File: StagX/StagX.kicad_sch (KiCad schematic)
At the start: 2 parts

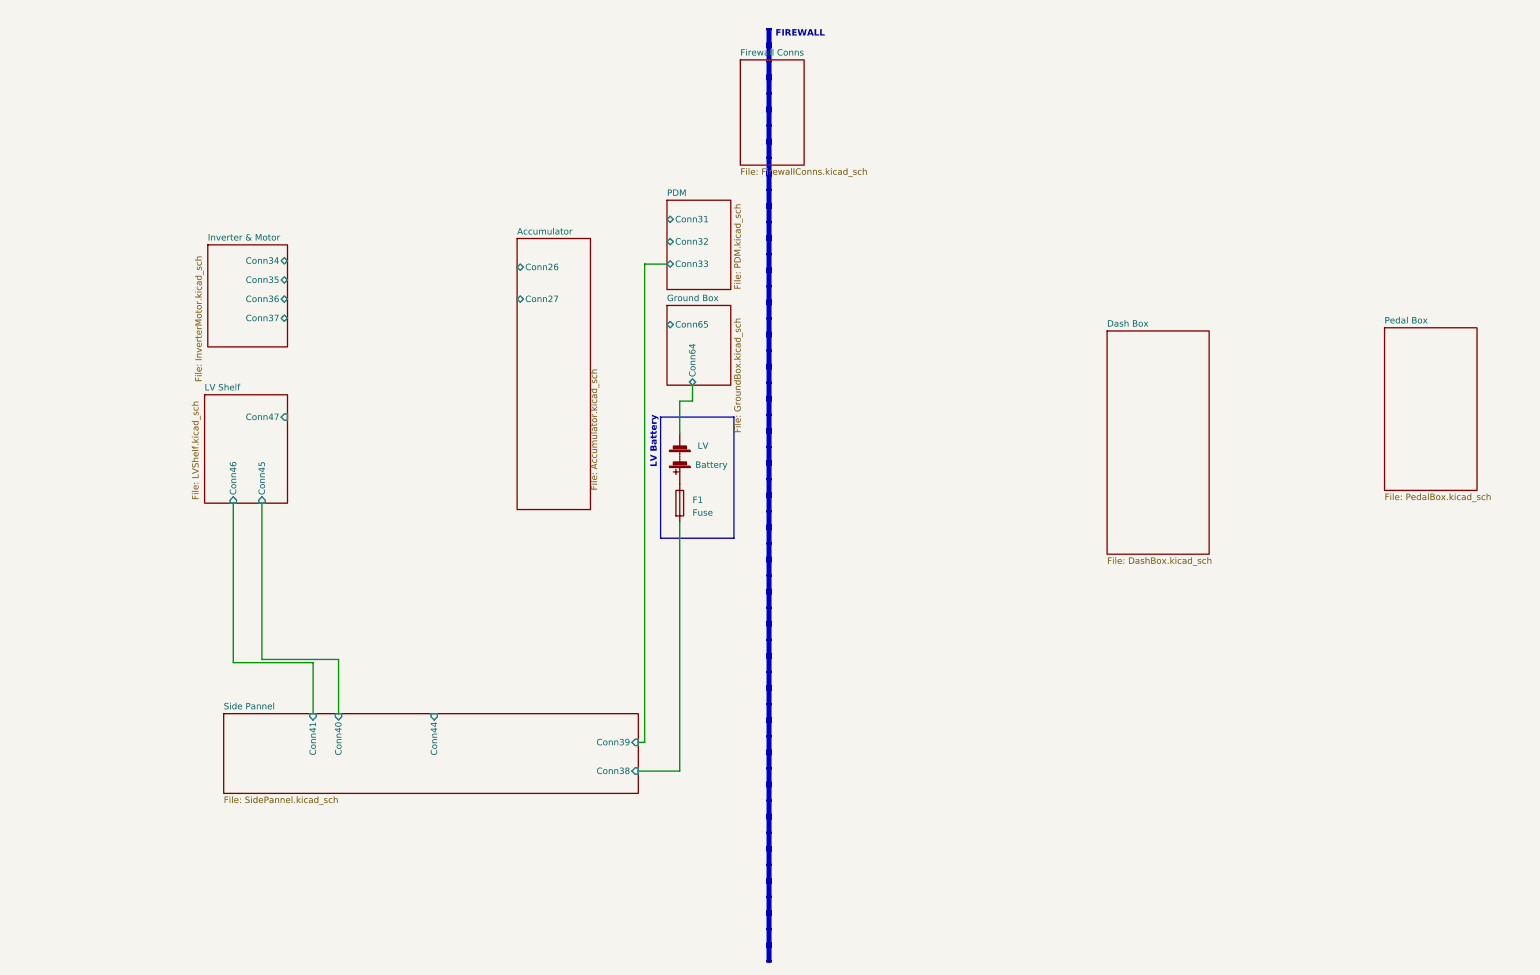
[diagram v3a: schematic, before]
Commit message: feat(RearLoom): completed Rear Electronics Box
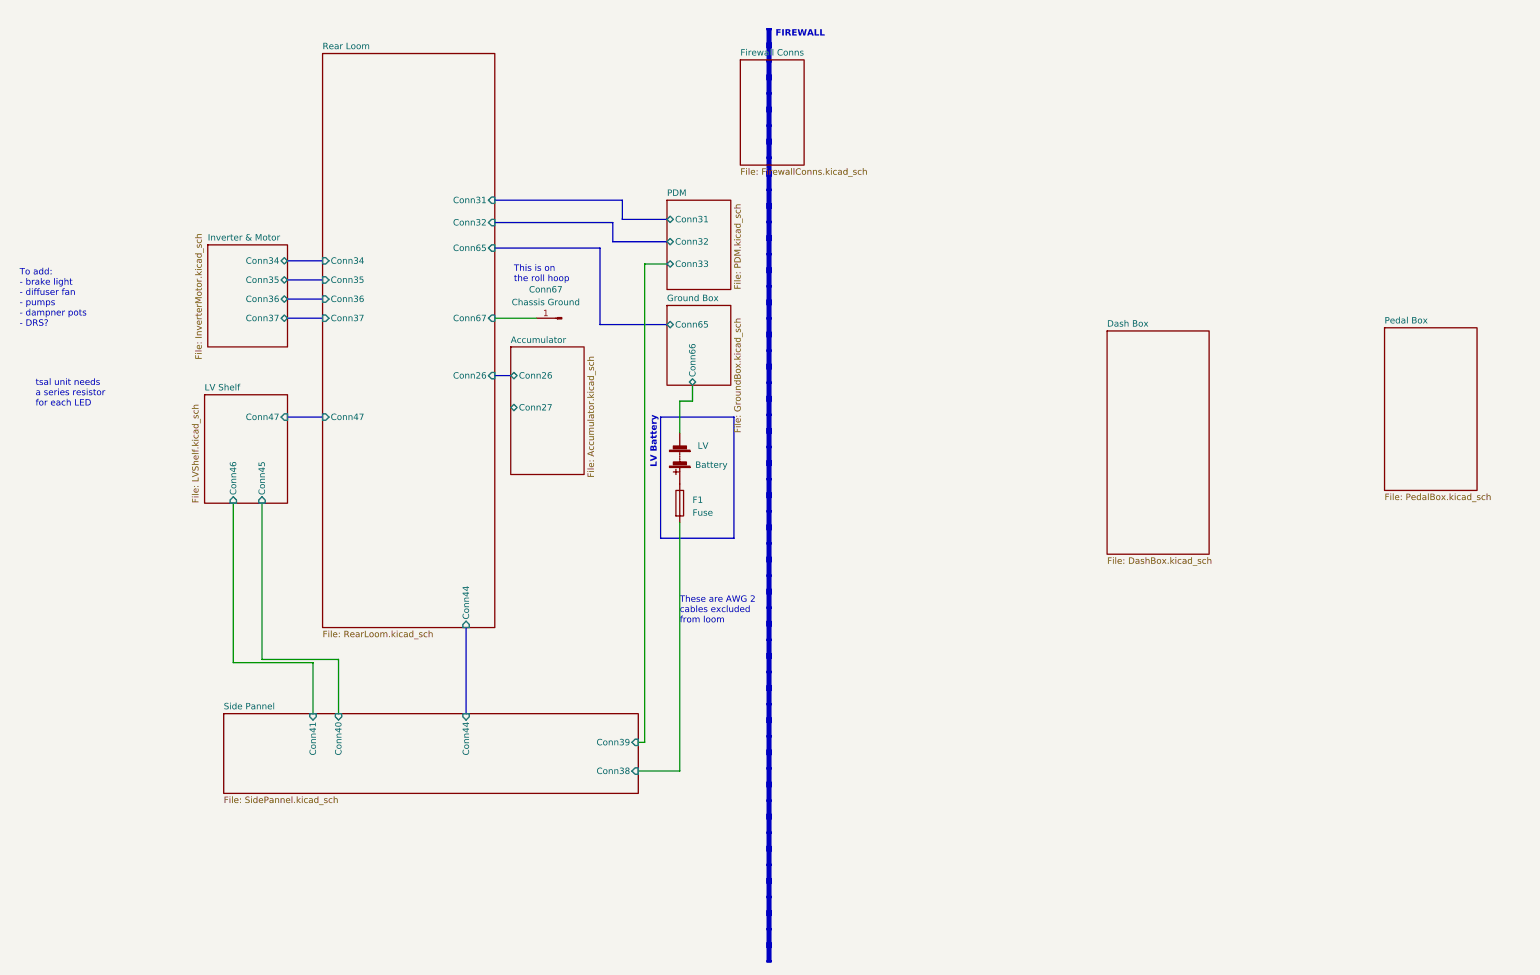
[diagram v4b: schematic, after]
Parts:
- added Conn67: Chassis Ground, symbol Connector:Conn_01x01_Pin
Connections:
- net Ground Box/Conn64 renamed Ground Box/Conn66
- new net Rear Loom/Conn67: Conn67.1 (Pin_1)
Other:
- added sheet Rear Loom (RearLoom.kicad_sch)
- sheet Ground Box ports: added Conn66; removed Conn64
- note added: "These are AWG 2 cables excluded from loom"
- note added: "This is on the roll hoop"
- note added: "To add: - brake light - diffuser fan - pumps - dampner pots - DRS?"
- note added: "tsal unit needs a series resistor for each LED"
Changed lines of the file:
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@@
     (comment 4 "N/A")
   )
+  (bus (pts (xy 99.06 51.435) (xy 99.06 55.245))
+    (stroke (width 0) (type default))
+  )
+  (bus (pts (xy 75.565 56.515) (xy 96.52 56.515))
+    (stroke (width 0) (type default))
+  )
   (wire (pts (xy 112.395 86.995) (xy 114.935 86.995))
     (stroke (width 0) (type default))
   )
+  (bus (pts (xy 34.29 66.675) (xy 41.275 66.675))
+    (stroke (width 0) (type default))
+  )
   (wire (pts (xy 39.37 149.225) (xy 39.37 139.065))
     (stroke (width 0) (type default))
   )
+  (bus (pts (xy 99.06 55.245) (xy 109.855 55.245))
+    (stroke (width 0) (type default))
+  )
   (wire (pts (xy 29.21 138.43) (xy 29.21 107.315))
     (stroke (width 0) (type default))
   )
+  (bus (pts (xy 34.29 59.055) (xy 41.275 59.055))
+    (stroke (width 0) (type default))
+  )
+  (bus (pts (xy 34.29 90.17) (xy 41.275 90.17))
+    (stroke (width 0) (type default))
+  )
+  (bus (pts (xy 75.565 51.435) (xy 99.06 51.435))
+    (stroke (width 0) (type default))
+  )
+  (bus (pts (xy 100.965 46.99) (xy 100.965 50.8))
+    (stroke (width 0) (type default))
+  )
   (wire (pts (xy 112.395 160.655) (xy 104.14 160.655))
     (stroke (width 0) (type default))
@@
     (stroke (width 0) (type default))
   )
+  (bus (pts (xy 69.85 132.08) (xy 69.85 149.225))
+    (stroke (width 0) (type default))
+  )
   (wire (pts (xy 23.495 107.315) (xy 23.495 139.065))
     (stroke (width 0) (type default))
   )
+  (bus (pts (xy 75.565 46.99) (xy 100.965 46.99))
+    (stroke (width 0) (type default))
+  )
+  (bus (pts (xy 96.52 56.515) (xy 96.52 71.755))
+    (stroke (width 0) (type default))
+  )
   (wire (pts (xy 44.45 138.43) (xy 29.21 138.43))
     (stroke (width 0) (type default))
   )
+  (bus (pts (xy 100.965 50.8) (xy 109.855 50.8))
+    (stroke (width 0) (type default))
+  )
   (wire (pts (xy 112.395 111.125) (xy 112.395 160.655))
     (stroke (width 0) (type default))
   )
+  (bus (pts (xy 75.565 81.915) (xy 78.74 81.915))
+    (stroke (width 0) (type default))
+  )
+  (bus (pts (xy 34.29 70.485) (xy 41.275 70.485))
+    (stroke (width 0) (type default))
+  )
   (wire (pts (xy 39.37 139.065) (xy 23.495 139.065))
     (stroke (width 0) (type default))
@@
   )
   (wire (pts (xy 105.41 59.69) (xy 109.855 59.69))
+    (stroke (width 0) (type default))
+  )
+  (bus (pts (xy 34.29 62.865) (xy 41.275 62.865))
+    (stroke (width 0) (type default))
+  )
+  (bus (pts (xy 96.52 71.755) (xy 109.855 71.755))
+    (stroke (width 0) (type default))
+  )
+  (wire (pts (xy 75.565 70.485) (xy 83.82 70.485))
     (stroke (width 0) (type default))
   )
@@
     (fill (type none))
   )
+  (text "To add:\n- brake light\n- diffuser fan\n- pumps\n- dampner pots\n- DRS?\n"
+    (at -19.05 72.39 0)
+    (effects (font (size 1.27 1.27)) (justify left bottom))
+  )
+  (text "This is on\nthe roll hoop" (at 79.375 63.5 0)
+    (effects (font (size 1.27 1.27)) (justify left bottom))
+  )
+  (text "These are AWG 2\ncables excluded\nfrom loom" (at 112.395 131.445 0)
+    (effects (font (size 1.27 1.27)) (justify left bottom))
+  )
   (text "LV Battery" (at 107.95 100.33 90)
     (effects (font (size 1.27 1.27) bold (color 0 0 0 1)) (justify left bottom))
@@
   (text "FIREWALL" (at 131.445 14.605 0)
     (effects (font (size 1.27 1.27) (thickness 0.254) bold (color 255 0 0 1)) (justify left bottom))
+  )
+  (text "tsal unit needs \na series resistor\nfor each LED" (at -15.875 88.265 0)
+    (effects (font (size 1.27 1.27)) (justify left bottom))
   )
   (symbol (lib_id "Device:Fuse") (at 112.395 107.315 0) (unit 1)
@@
     )
   )
+  (symbol (lib_id "Connector:Conn_01x01_Pin") (at 88.9 70.485 180) (unit 1)
+    (in_bom yes) (on_board yes) (dnp no)
+    (property "Reference" "Conn67" (at 85.725 64.77 0)
+      (effects (font (size 1.27 1.27)))
+    )
+    (property "Value" "Chassis Ground" (at 85.725 67.31 0)
+      (effects (font (size 1.27 1.27)))
+    )
+    (property "Footprint" "" (at 88.9 70.485 0)
+      (effects (font (size 1.27 1.27)) hide)
+    )
+    (property "Datasheet" "~" (at 88.9 70.485 0)
+      (effects (font (size 1.27 1.27)) hide)
+    )
+    (pin "1")
+    (instances
+      (project "StagX"
+        (path "/f802a14a-9970-4775-97a5-629bebb8e9f9"
+          (reference "Conn67") (unit 1)
+        )
+      )
+    )
+  )
   (symbol (lib_id "Device:Battery") (at 112.395 98.425 180) (unit 1)
     (in_bom yes) (on_board yes) (dnp no)
@@
       (effects (font (size 1.27 1.27)) (justify left bottom))
     )
-    (property "Sheetfile" "InverterMotor.kicad_sch" (at 15.875 83.185 90)
+    (property "Sheetfile" "InverterMotor.kicad_sch" (at 15.875 78.74 90)
       (effects (font (size 1.27 1.27)) (justify left top))
     )
@@
       (effects (font (size 1.27 1.27)) (justify left bottom))
     )
-    (property "Sheetfile" "LVShelf.kicad_sch" (at 15.24 106.68 90)
+    (property "Sheetfile" "LVShelf.kicad_sch" (at 15.24 107.315 90)
       (effects (font (size 1.27 1.27)) (justify left top))
     )
@@
     )
   )
-  (sheet (at 80.01 54.61) (size 14.605 53.975)
-    (stroke (width 0.1524) (type solid) (color 255 0 0 1))
-    (fill (color 0 0 0 0.0000))
-    (property "Sheetname" "Accumulator" (at 80.01 53.975 0)
-      (effects (font (size 1.27 1.27)) (justify left bottom))
-    )
-    (property "Sheetfile" "Accumulator.kicad_sch" (at 94.615 104.775 90)
-      (effects (font (size 1.27 1.27)) (justify left top))
-    )
-    (pin "Conn26" bidirectional (at 80.01 60.325 180)
-      (effects (font (size 1.27 1.27)) (justify left))
-    )
-    (pin "Conn27" bidirectional (at 80.01 66.675 180)
+  (sheet (at 78.74 76.2) (size 14.605 25.4)
+    (stroke (width 0.1524) (type solid) (color 255 0 0 1))
+    (fill (color 0 0 0 0.0000))
+    (property "Sheetname" "Accumulator" (at 78.74 75.565 0)
+      (effects (font (size 1.27 1.27)) (justify left bottom))
+    )
+    (property "Sheetfile" "Accumulator.kicad_sch" (at 93.98 102.235 90)
+      (effects (font (size 1.27 1.27)) (justify left top))
+    )
+    (pin "Conn26" bidirectional (at 78.74 81.915 180)
+      (effects (font (size 1.27 1.27)) (justify left))
+    )
+    (pin "Conn27" bidirectional (at 78.74 88.265 180)
       (effects (font (size 1.27 1.27)) (justify left))
     )
@@
       (effects (font (size 1.27 1.27)) (justify right))
     )
-    (pin "Conn44" input (at 63.5 149.225 90)
+    (pin "Conn44" input (at 69.85 149.225 90)
       (effects (font (size 1.27 1.27)) (justify right))
     )
@@
     )
   )
+  (sheet (at 41.275 17.78) (size 34.29 114.3) (fields_autoplaced)
+    (stroke (width 0.1524) (type solid) (color 0 0 255 1))
+    (fill (color 0 0 0 0.0000))
+    (property "Sheetname" "Rear Loom" (at 41.275 17.0684 0)
+      (effects (font (size 1.27 1.27)) (justify left bottom))
+    )
+    (property "Sheetfile" "RearLoom.kicad_sch" (at 41.275 132.6646 0)
+      (effects (font (size 1.27 1.27)) (justify left top))
+    )
+    (pin "Conn44" input (at 69.85 132.08 270)
+      (effects (font (size 1.27 1.27)) (justify left))
+    )
+    (pin "Conn34" input (at 41.275 59.055 180)
+      (effects (font (size 1.27 1.27)) (justify left))
+    )
+    (pin "Conn36" input (at 41.275 66.675 180)
+      (effects (font (size 1.27 1.27)) (justify left))
+    )
+    (pin "Conn47" input (at 41.275 90.17 180)
+      (effects (font (size 1.27 1.27)) (justify left))
+    )
+    (pin "Conn37" input (at 41.275 70.485 180)
+      (effects (font (size 1.27 1.27)) (justify left))
+    )
+    (pin "Conn26" input (at 75.565 81.915 0)
+      (effects (font (size 1.27 1.27)) (justify right))
+    )
+    (pin "Conn35" input (at 41.275 62.865 180)
+      (effects (font (size 1.27 1.27)) (justify left))
+    )
+    (pin "Conn31" input (at 75.565 46.99 0)
+      (effects (font (size 1.27 1.27)) (justify right))
+    )
+    (pin "Conn32" input (at 75.565 51.435 0)
+      (effects (font (size 1.27 1.27)) (justify right))
+    )
+    (pin "Conn65" input (at 75.565 56.515 0)
+      (effects (font (size 1.27 1.27)) (justify right))
+    )
+    (pin "Conn67" input (at 75.565 70.485 0)
+      (effects (font (size 1.27 1.27)) (justify right))
+    )
+    (instances
+      (project "StagX"
+        (path "/f802a14a-9970-4775-97a5-629bebb8e9f9" (page "12"))
+      )
+    )
+  )
   (sheet (at 109.855 67.945) (size 12.7 15.875)
     (stroke (width 0.1524) (type solid) (color 255 0 0 1))
@@
       (effects (font (size 1.27 1.27)) (justify left top))
     )
-    (pin "Conn64" bidirectional (at 114.935 83.82 270)
-      (effects (font (size 1.27 1.27)) (justify left))
-    )
+    (pin "Conn66" bidirectional (at 114.935 83.82 270)
+      (effects (font (size 1.27 1.27)) (justify left))
+    )

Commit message: feat(RearLoom): completed Inverter, Motor and Resolver sheet
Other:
- sheet Inverter & Motor ports: added Conn68; removed none
- sheet Rear Loom ports: added Conn68; removed none
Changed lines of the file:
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@@
+    (stroke (width 0) (type default))
+  )
+  (bus (pts (xy 34.29 73.66) (xy 41.275 73.66))
     (stroke (width 0) (type default))
   )
@@
       (effects (font (size 1.27 1.27)) (justify right))
     )
+    (pin "Conn68" bidirectional (at 34.29 73.66 0)
+      (effects (font (size 1.27 1.27)) (justify right))
+    )
     (instances
       (project "StagX"
@@
       (effects (font (size 1.27 1.27)) (justify right))
     )
-    (instances
+    (pin "Conn68" input (at 41.275 73.66 180)
+      (effects (font (size 1.27 1.27)) (justify left))
+    )
+    (instances

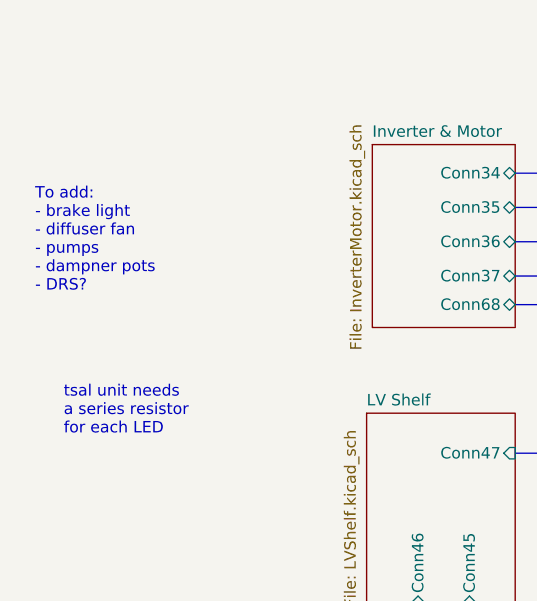
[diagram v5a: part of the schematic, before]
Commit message: feat(RearLoom): progress with Rear Loom. Miising Power and GND
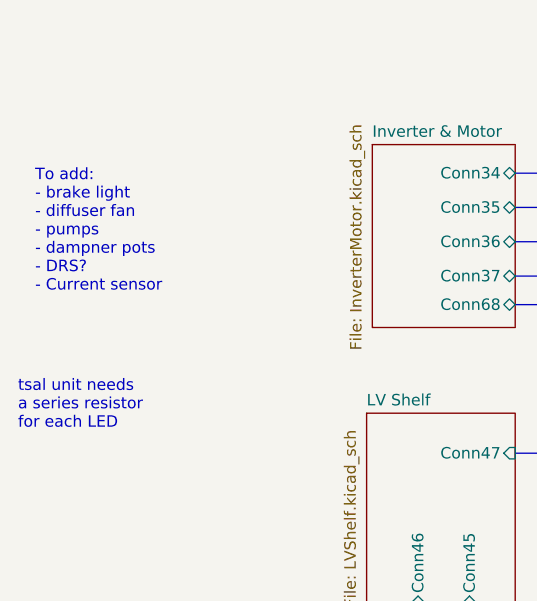
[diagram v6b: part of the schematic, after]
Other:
- note added: "To add: - brake light - diffuser fan - pumps - dampner pots - DRS? - Current sensor"
- note removed: "To add: - brake light - diffuser fan - pumps - dampner pots - DRS?"
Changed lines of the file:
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@@
     (fill (type none))
   )
-  (text "To add:\n- brake light\n- diffuser fan\n- pumps\n- dampner pots\n- DRS?\n"
+  (text "To add:\n- brake light\n- diffuser fan\n- pumps\n- dampner pots\n- DRS?\n- Current sensor"
     (at -19.05 72.39 0)
     (effects (font (size 1.27 1.27)) (justify left bottom))
@@
     (effects (font (size 1.27 1.27) (thickness 0.254) bold (color 255 0 0 1)) (justify left bottom))
   )
-  (text "tsal unit needs \na series resistor\nfor each LED" (at -15.875 88.265 0)
+  (text "tsal unit needs \na series resistor\nfor each LED" (at -20.955 87.63 0)
     (effects (font (size 1.27 1.27)) (justify left bottom))
   )
